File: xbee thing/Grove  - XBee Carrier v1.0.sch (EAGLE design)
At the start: 44 parts, among them J1 SULLINS_NPPN101BFCN-RCSULLINS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, J2 HEADER-10P_STANDARD, J3 HEADER-10P_STANDARD, J4 SULLINS_NPPN101BFCN-RCSULLINS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, Q4 FQ7050B-6.000, U1 TUSB2046BVF, U2 RT9167A_33PB, U4 FT232RL

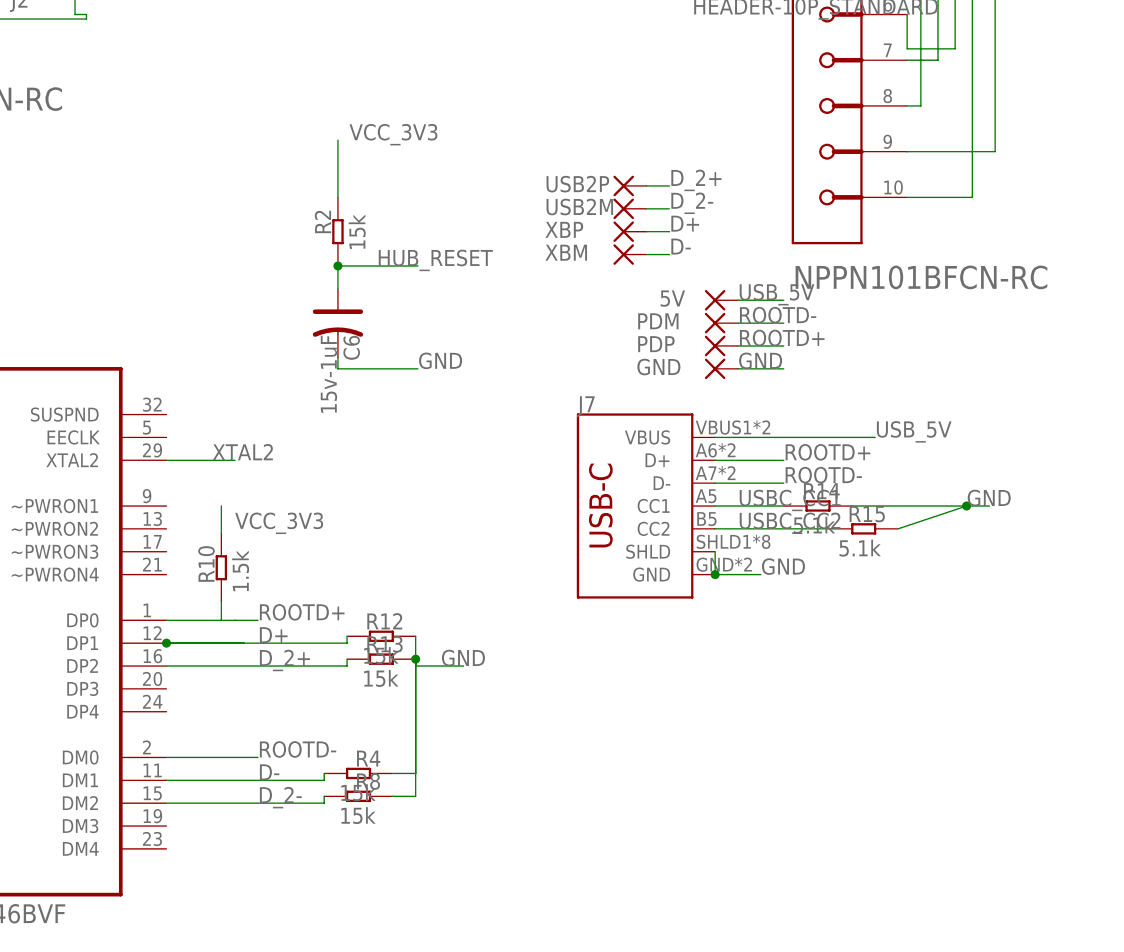
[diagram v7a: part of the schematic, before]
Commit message: add more resistors in series to Root D+ and D- pins
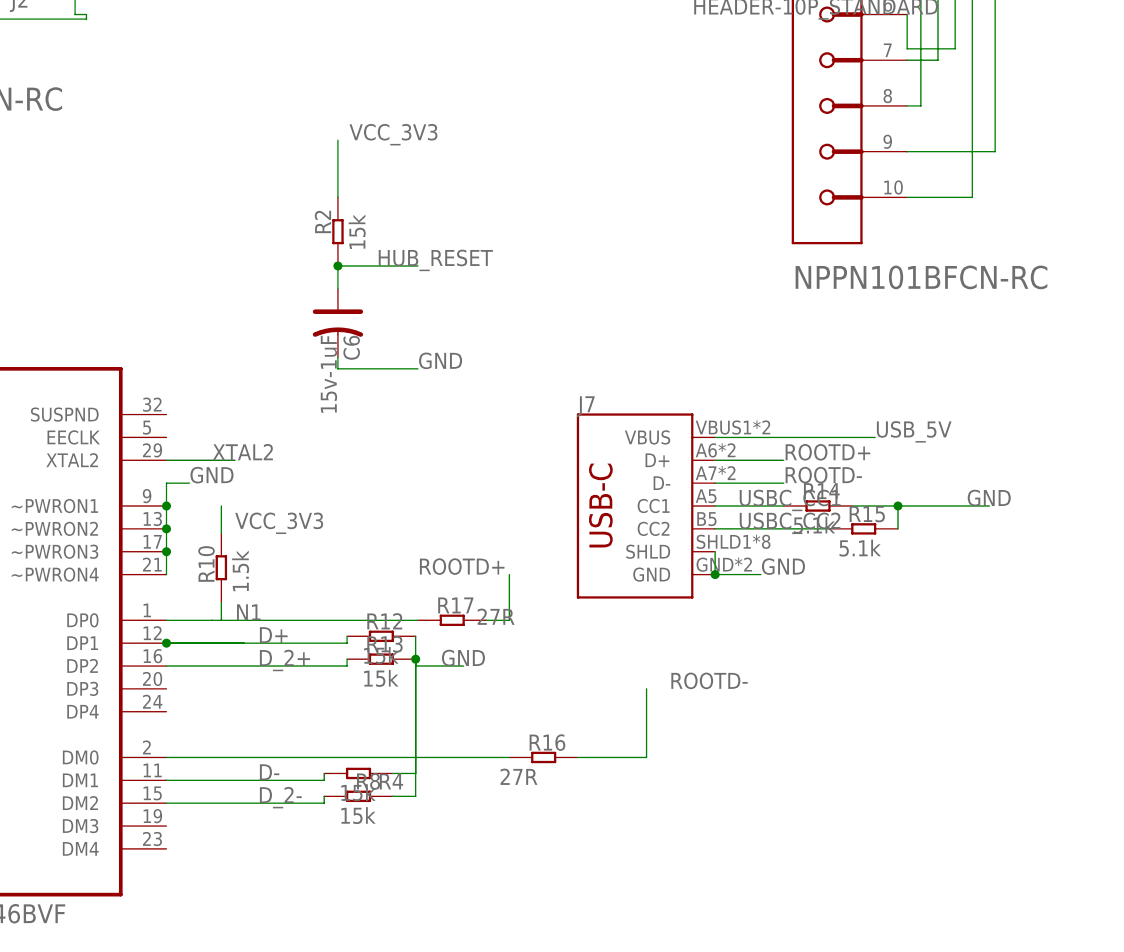
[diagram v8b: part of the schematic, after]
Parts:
- removed 5V, GND, PDM, PDP, USB2M, USB2P, XBM, XBP: (no value), wirepad:2,15/1,0
- added R16, R17: 27R, discrete:R-0603
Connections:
- new net N$5: R16.2, U1.DM0
- new net N1: R10.2, R17.2, U1.DP0
- net D+: no longer XBP.P
- net D-: no longer XBM.P
- net D_2+: no longer USB2P.P
- net D_2-: no longer USB2M.P
- net GND: now also U1.~PWRON1, U1.~PWRON2, U1.~PWRON3, U1.~PWRON4; no longer GND.P
- net ROOTD+: now also R17.1; no longer PDP.P, R10.2, U1.DP0
- net ROOTD-: now also R16.1; no longer PDM.P, U1.DM0
- net USB_5V: no longer 5V.P
